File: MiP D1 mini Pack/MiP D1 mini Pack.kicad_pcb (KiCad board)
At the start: 2 copper layers, 41.4 x 63.8 mm, 15 parts, among them J1 MiP, J2 Debug, U1 WEMOS D1 mini, U2 74LVC1G125

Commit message: Remove title case
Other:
- board text added: "MiP D1 mini pack"
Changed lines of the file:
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@@
 		)
 	)
-	(gr_text "MiP D1 mini Pack"
+	(gr_text "MiP D1 mini pack"
 		(at 148.4 115.6 0)
 		(layer "B.SilkS")

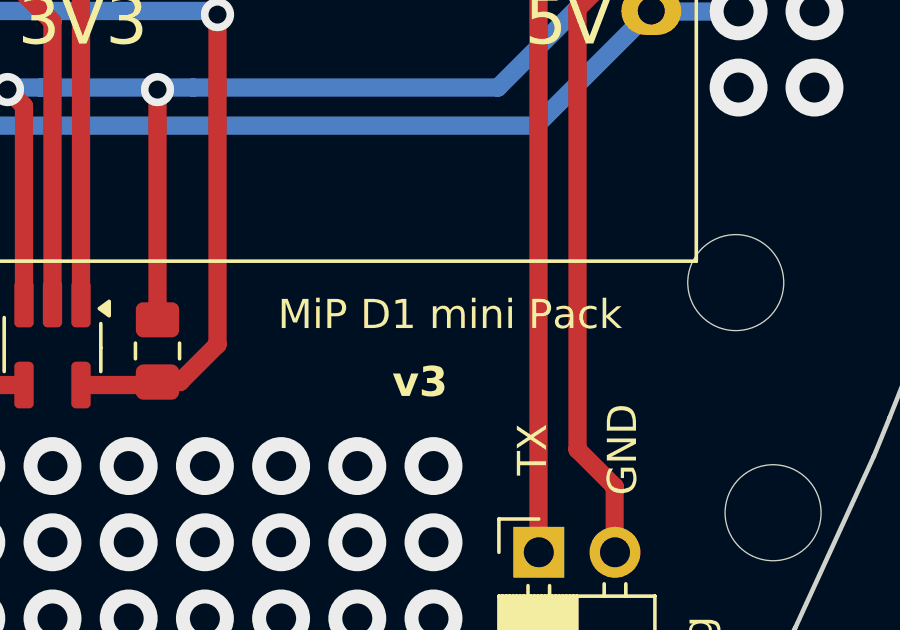
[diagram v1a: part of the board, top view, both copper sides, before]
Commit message: More title case
Not sure I even like calling it a "pack"
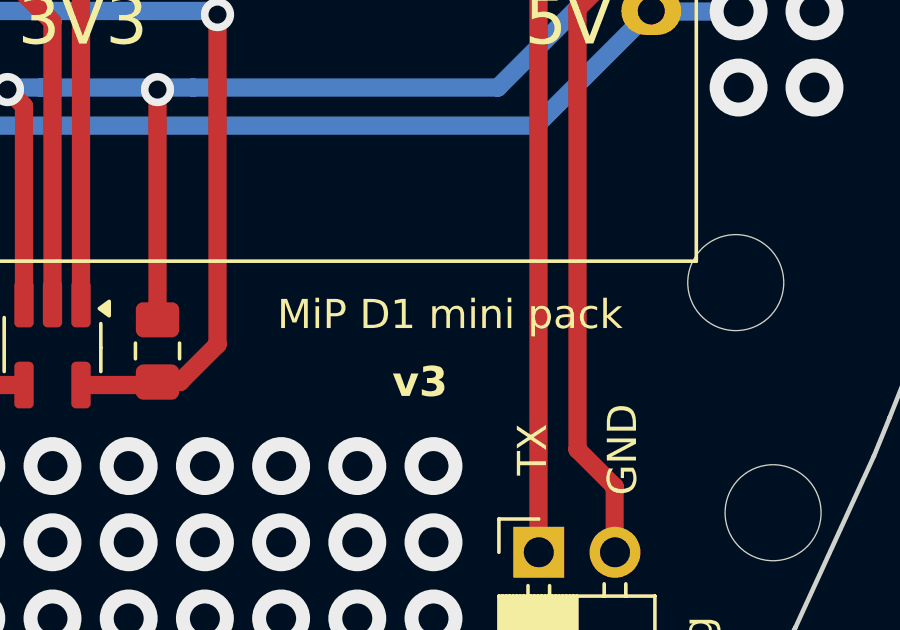
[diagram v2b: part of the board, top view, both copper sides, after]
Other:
- board text removed: "MiP D1 mini Pack"
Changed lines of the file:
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@@
 		)
 	)
-	(gr_text "MiP D1 mini Pack"
+	(gr_text "MiP D1 mini pack"
 		(at 153.25 116.5 0)
 		(layer "F.SilkS")
